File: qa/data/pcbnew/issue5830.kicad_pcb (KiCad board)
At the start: 4 copper layers, 20 x 100 mm, 22 parts, among them IC1 ATTINY441-SSU, P1 CONN_02X03, P2 CONN_01X04, X1 16MHz

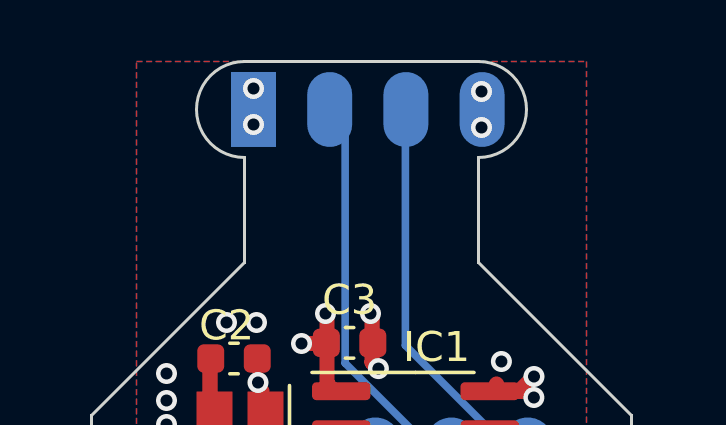
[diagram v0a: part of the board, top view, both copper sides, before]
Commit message: feat: update kicad to 9.0.0+dfsg-1
Signed-off-by: lhdjply <lhdjply@126.com>
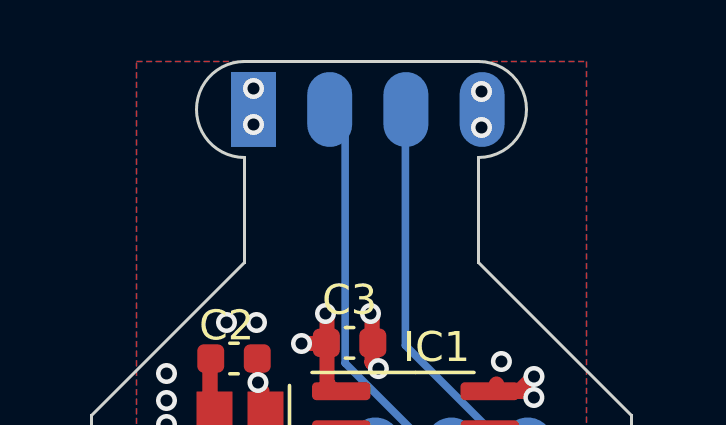
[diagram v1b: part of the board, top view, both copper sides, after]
